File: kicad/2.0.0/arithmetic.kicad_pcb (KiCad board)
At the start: 2 copper layers, 44.9 x 52.9 mm, 70 parts, among them J1 Conn_01x03_Male, J2 Conn_01x05_Male, J3 Conn_01x05_Male, J4 Conn_Coaxial, J5 Conn_Coaxial, J6 Conn_Coaxial, M2.5 MountingHole_2.7mm_M2.5_ISO73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, U1 LM317, U2 LM337, U3 OPA197xDBV, U4 OPA197xDBV, U5 OPA197xDBV

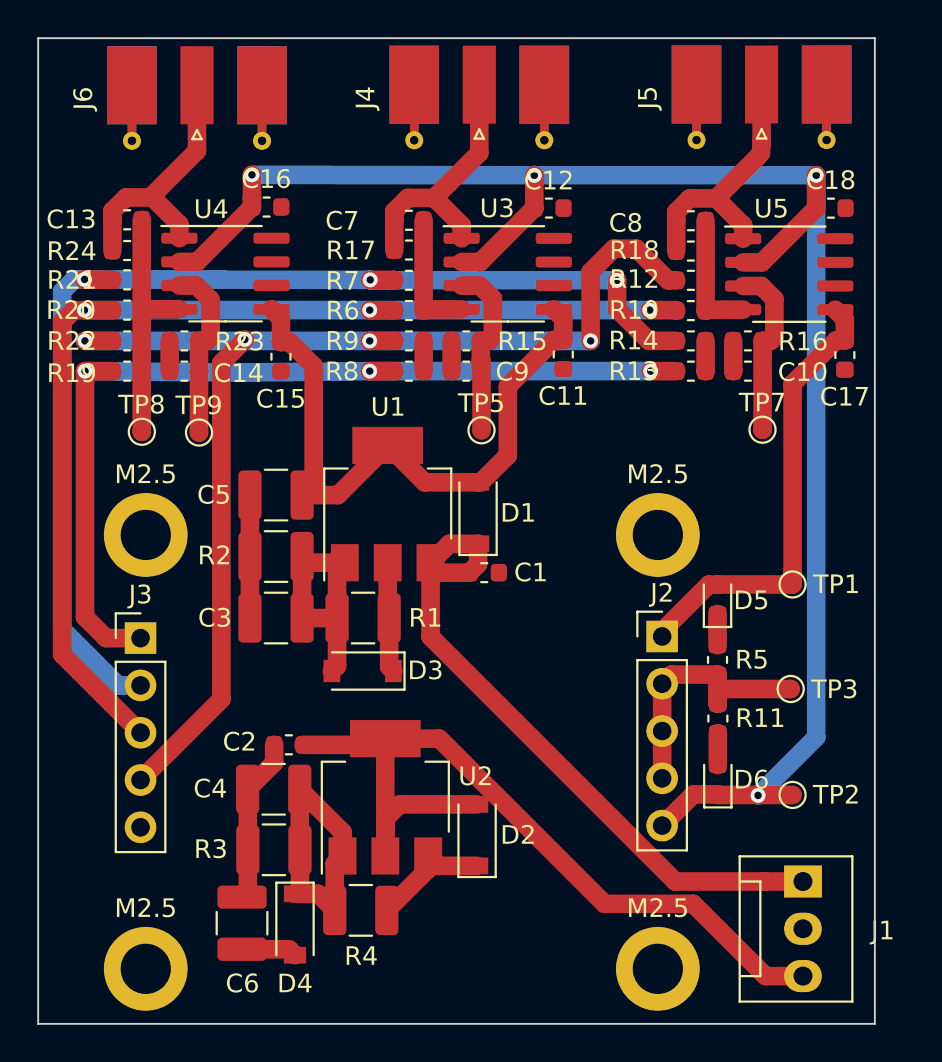
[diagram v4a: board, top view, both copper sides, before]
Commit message: completed arithmetic 2.0.0 pcb
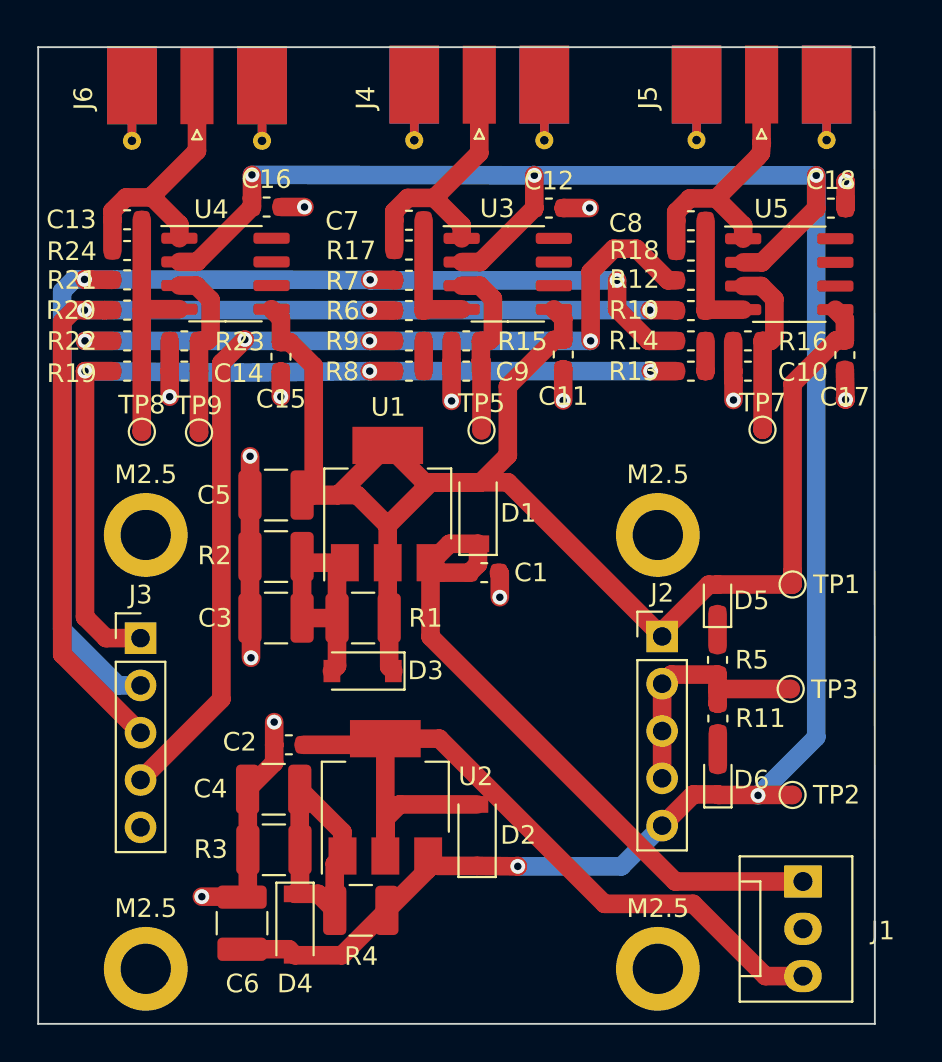
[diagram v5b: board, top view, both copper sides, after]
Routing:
- net +12V: track 65.3 -> 91.7 mm
- net GND: track 34.2 -> 57.4 mm, vias 0 -> 14
- net -12V: track 102.9 -> 119.7 mm, vias 4 -> 5
- added copper zone on In1.Cu, net GND
- added copper zone on In2.Cu, net GND
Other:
- board size 44.9 x 52.9 mm -> 44.9 x 52.5 mm
- copper layers 2 -> 4

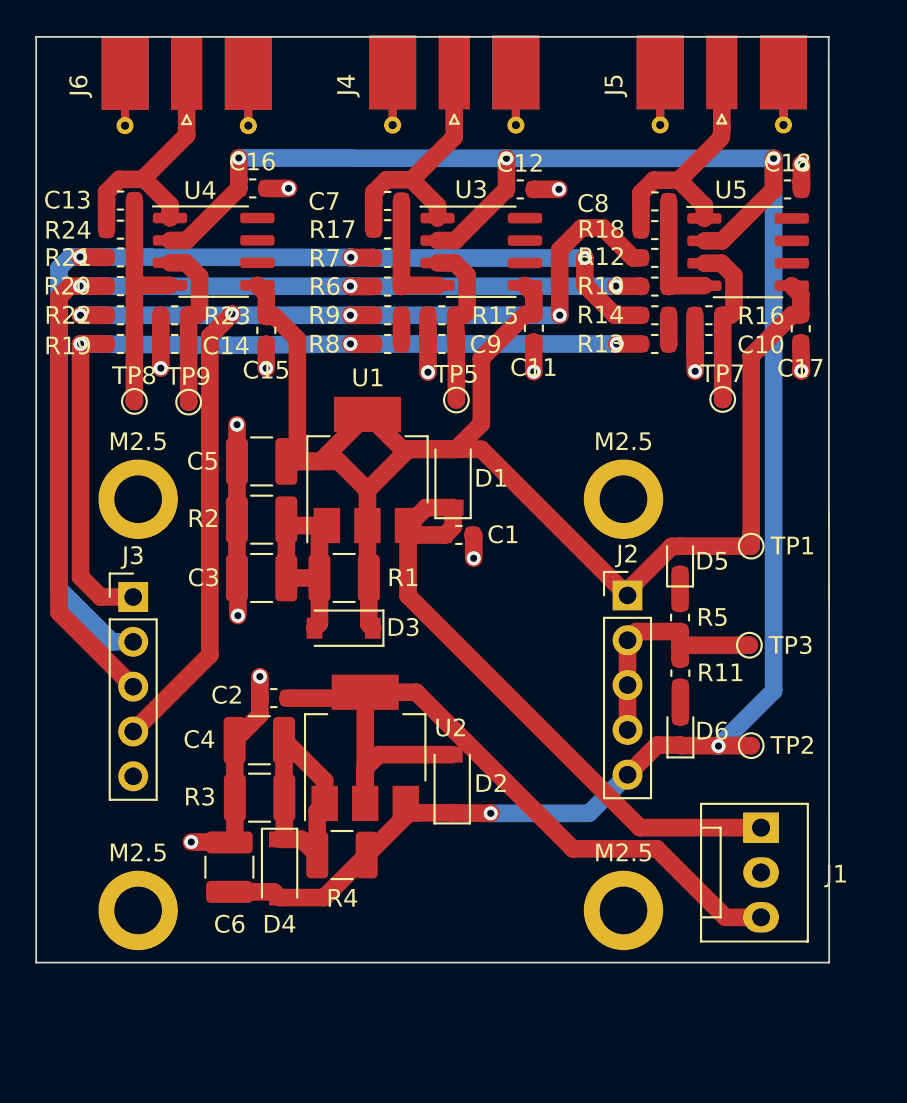
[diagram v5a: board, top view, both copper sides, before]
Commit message: completed redesign of arithmetic and detector 2.0.0 boards
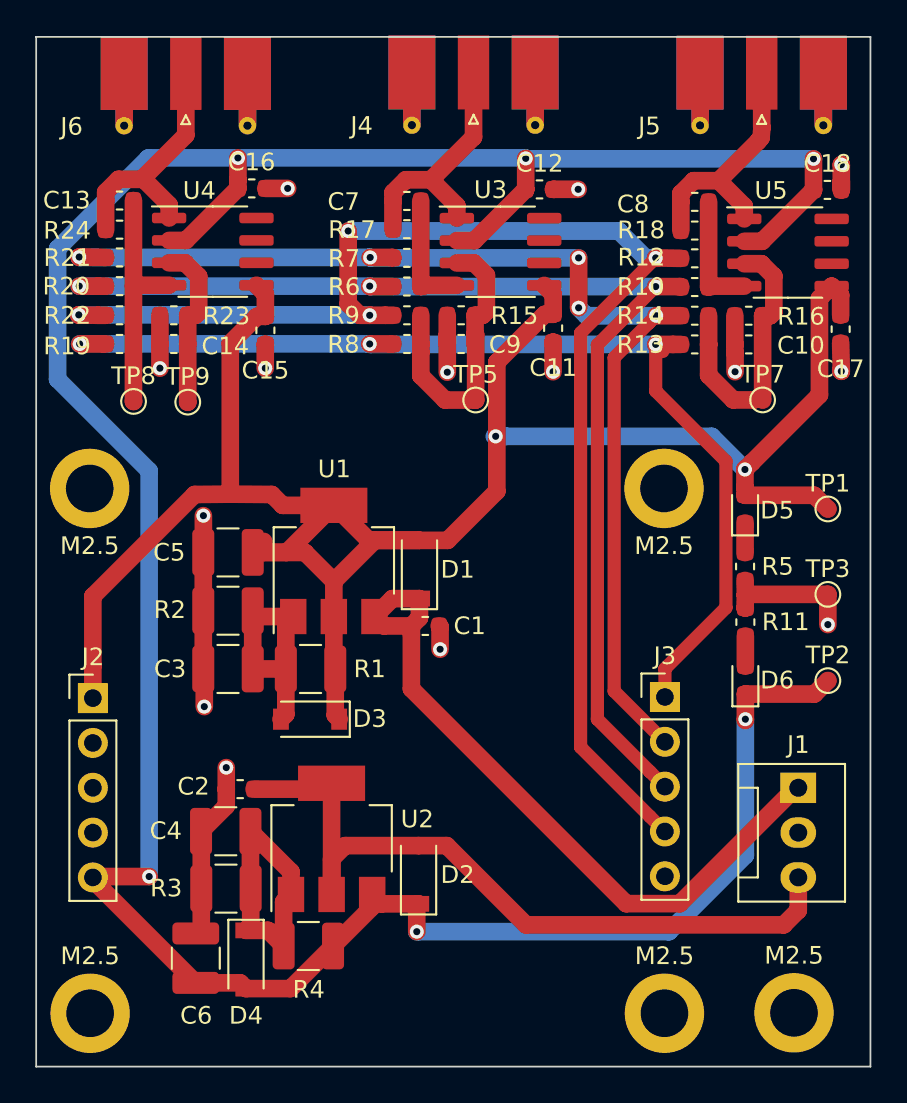
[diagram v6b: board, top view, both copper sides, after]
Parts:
- removed the M2.5 at (107.0, 127.0)
- removed the M2.5 at (79.5, 103.7)
- removed the M2.5 at (79.5, 127.0)
- removed the M2.5 at (107.0, 103.7)
- added M2.5: MountingHole_2.7mm_M2.5_ISO7380_Pad, MountingHole:MountingHole_2.7mm_M2.5_ISO7380_Pad, F.Cu at (116.7, 132.8)
- added M2.5: MountingHole_2.7mm_M2.5_ISO7380_Pad, MountingHole:MountingHole_2.7mm_M2.5_ISO7380_Pad, F.Cu at (109.4, 132.8)
- added M2.5: MountingHole_2.7mm_M2.5_ISO7380_Pad, MountingHole:MountingHole_2.7mm_M2.5_ISO7380_Pad, F.Cu at (76.8, 132.8)
- added M2.5: MountingHole_2.7mm_M2.5_ISO7380_Pad, MountingHole:MountingHole_2.7mm_M2.5_ISO7380_Pad, F.Cu at (76.8, 103.1)
- added M2.5: MountingHole_2.7mm_M2.5_ISO7380_Pad, MountingHole:MountingHole_2.7mm_M2.5_ISO7380_Pad, F.Cu at (109.3, 103.1)
- moved J2 30.8 mm to (77.0, 115.0)
- moved J3 30.7 mm to (109.4, 114.9)
- moved TP2 5.69 mm to (118.6, 114.0)
- moved C6 5.50 mm to (82.8, 129.7)
- moved U2 5.50 mm to (90.5, 122.9)
- moved C1 5.50 mm to (95.8, 110.9)
- moved C2 5.50 mm to (85.3, 120.1)
- moved C3 5.50 mm to (84.6, 113.3)
- moved C4 5.50 mm to (84.5, 122.5)
- moved C5 5.50 mm to (84.6, 106.7)
- moved D1 5.50 mm to (95.5, 107.7)
- moved D2 5.50 mm to (95.4, 125.0)
- moved D3 5.50 mm to (89.3, 116.2)
- moved D4 5.50 mm to (85.6, 129.8)
- moved R1 5.50 mm to (89.3, 113.3)
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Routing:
- net -12V: track 119.7 -> 166.8 mm, vias 5 -> 6
- net GND: track 57.4 -> 100.4 mm
- net +12V: track 91.7 -> 121.3 mm, vias 0 -> 2
- net /-Y2: track 65.8 -> 80.7 mm
- net /-X1: track 51.3 -> 60.5 mm
- net /-X2: track 59.9 -> 68.2 mm
- net Net-(C9-Pad2): track 11.8 -> 17.2 mm
- net Net-(C10-Pad2): track 11.1 -> 16.0 mm
- net /-Y1: track 62.0 -> 66.3 mm, vias 3 -> 5
- net +15V: track 36.4 -> 40.3 mm
- net -15V: track 45.8 -> 43.7 mm
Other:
- board size 44.9 x 52.5 mm -> 47.3 x 58.3 mm
